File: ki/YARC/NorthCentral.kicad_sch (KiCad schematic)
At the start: 9 parts, among them U102 74HC245, U103 74HC245, U106 74LS139, U128 74LS157, U132 74LS157, U133 74LS21, U134 74LS32

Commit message: Ongoing corrections and improvements
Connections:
- net KX_HI_CLK renamed ~{KX_HI_OE}
- net KX_LO_CLK renamed ~{KX_LO_OE}
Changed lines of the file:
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@@
     )
   )
-  (global_label "KX_LO_CLK" (shape input) (at 203.2 73.66 0) (fields_autoplaced)
+  (global_label "~{KX_LO_OE}" (shape input) (at 203.2 73.66 0) (fields_autoplaced)
     (effects (font (size 1.27 1.27)) (justify left))
-    (property "Intersheet References" "${INTERSHEET_REFS}" (id 0) (at 215.9545 73.5806 0)
+    (property "Intersheet References" "${INTERSHEET_REFS}" (id 0) (at 214.866 73.5806 0)
       (effects (font (size 1.27 1.27)) (justify left) hide)
     )
@@
     )
   )
-  (global_label "KX_HI_CLK" (shape input) (at 203.2 88.9 0) (fields_autoplaced)
+  (global_label "~{KX_HI_OE}" (shape input) (at 203.2 88.9 0) (fields_autoplaced)
     (effects (font (size 1.27 1.27)) (justify left))
-    (property "Intersheet References" "${INTERSHEET_REFS}" (id 0) (at 215.5312 88.8206 0)
+    (property "Intersheet References" "${INTERSHEET_REFS}" (id 0) (at 214.4426 88.8206 0)
       (effects (font (size 1.27 1.27)) (justify left) hide)
     )

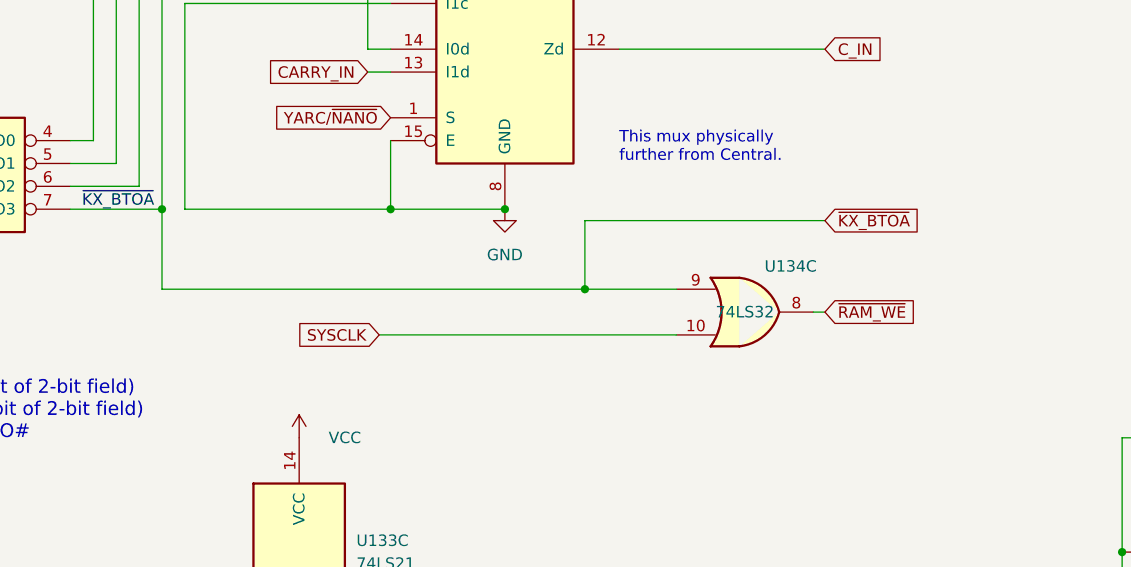
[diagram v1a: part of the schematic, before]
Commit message: Add the ACN mini-bus which can come from the instruction bits 11:8 or from the microcode bits 23:20. It selects the ALU operation and the condition codes.
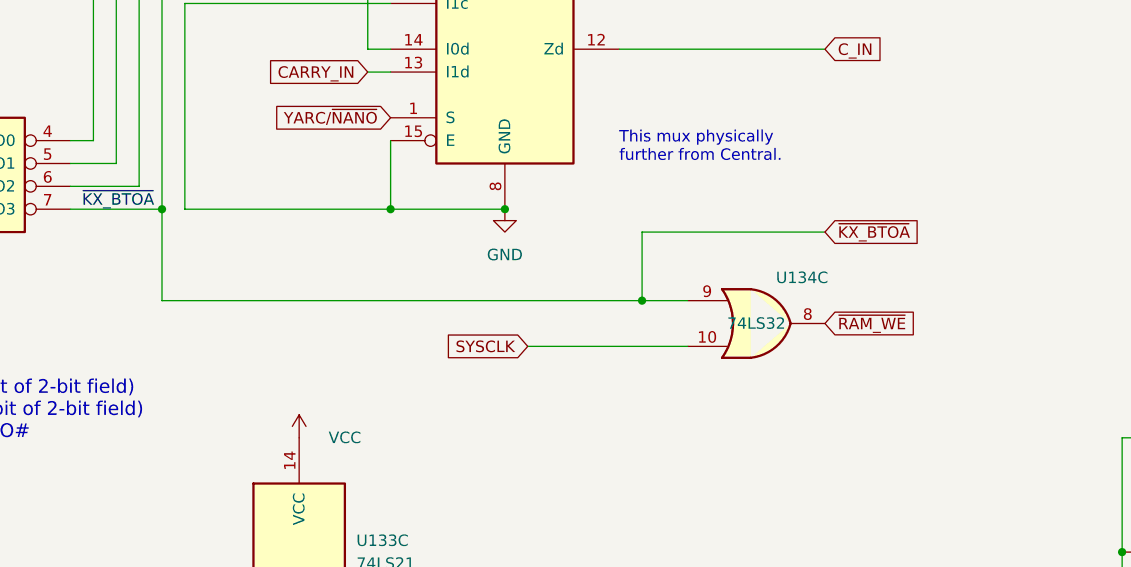
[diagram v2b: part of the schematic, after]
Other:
- moved on the sheet: U134C
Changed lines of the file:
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@@
   (junction (at 132.08 63.5) (diameter 0) (color 0 0 0 0)
   )
+  (junction (at 182.88 149.86) (diameter 0) (color 0 0 0 0)
+  )
   (junction (at 149.86 114.3) (diameter 0) (color 0 0 0 0)
   )
@@
   (junction (at 167.64 139.7) (diameter 0) (color 0 0 0 0)
   )
-  (junction (at 176.53 148.59) (diameter 0) (color 0 0 0 0)
-  )
   (junction (at 129.54 106.68) (diameter 0) (color 0 0 0 0)
   )
@@
     (stroke (width 0) (type default) (color 0 0 0 0))
   )
-  (wire (pts (xy 176.53 140.97) (xy 176.53 148.59))
-    (stroke (width 0) (type default) (color 0 0 0 0))
-  )
   (wire (pts (xy 119.38 139.7) (xy 129.54 139.7))
     (stroke (width 0) (type default) (color 0 0 0 0))
@@
     (stroke (width 0) (type default) (color 0 0 0 0))
   )
-  (wire (pts (xy 201.93 151.13) (xy 203.2 151.13))
-    (stroke (width 0) (type default) (color 0 0 0 0))
-  )
   (wire (pts (xy 134.62 101.6) (xy 134.62 91.44))
     (stroke (width 0) (type default) (color 0 0 0 0))
   )
+  (wire (pts (xy 187.96 154.94) (xy 170.18 154.94))
+    (stroke (width 0) (type default) (color 0 0 0 0))
+  )
   (wire (pts (xy 154.94 124.46) (xy 152.4 124.46))
     (stroke (width 0) (type default) (color 0 0 0 0))
@@
     (stroke (width 0) (type default) (color 0 0 0 0))
   )
+  (wire (pts (xy 187.96 149.86) (xy 182.88 149.86))
+    (stroke (width 0) (type default) (color 0 0 0 0))
+  )
   (wire (pts (xy 167.64 17.78) (xy 167.64 21.59))
     (stroke (width 0) (type default) (color 0 0 0 0))
@@
     (stroke (width 0) (type default) (color 0 0 0 0))
   )
-  (wire (pts (xy 186.69 148.59) (xy 176.53 148.59))
-    (stroke (width 0) (type default) (color 0 0 0 0))
-  )
   (bus (pts (xy 22.86 20.32) (xy 22.86 25.4))
     (stroke (width 0) (type default) (color 0 0 0 0))
@@
     (stroke (width 0) (type default) (color 0 0 0 0))
   )
+  (wire (pts (xy 182.88 142.24) (xy 182.88 149.86))
+    (stroke (width 0) (type default) (color 0 0 0 0))
+  )
   (wire (pts (xy 27.94 20.32) (xy 53.34 20.32))
     (stroke (width 0) (type default) (color 0 0 0 0))
@@
     (stroke (width 0) (type default) (color 0 0 0 0))
   )
+  (wire (pts (xy 203.2 142.24) (xy 182.88 142.24))
+    (stroke (width 0) (type default) (color 0 0 0 0))
+  )
   (bus (pts (xy 78.74 160.02) (xy 78.74 162.56))
     (stroke (width 0) (type default) (color 0 0 0 0))
@@
     (stroke (width 0) (type default) (color 0 0 0 0))
   )
-  (wire (pts (xy 129.54 148.59) (xy 129.54 139.7))
+  (wire (pts (xy 129.54 139.7) (xy 129.54 149.86))
     (stroke (width 0) (type default) (color 0 0 0 0))
   )
@@
     (stroke (width 0) (type default) (color 0 0 0 0))
   )
-  (wire (pts (xy 153.67 153.67) (xy 186.69 153.67))
-    (stroke (width 0) (type default) (color 0 0 0 0))
-  )
   (wire (pts (xy 81.28 139.7) (xy 93.98 139.7))
     (stroke (width 0) (type default) (color 0 0 0 0))
@@
     (stroke (width 0) (type default) (color 0 0 0 0))
   )
+  (wire (pts (xy 182.88 149.86) (xy 129.54 149.86))
+    (stroke (width 0) (type default) (color 0 0 0 0))
+  )
   (wire (pts (xy 152.4 121.92) (xy 152.4 114.3))
     (stroke (width 0) (type default) (color 0 0 0 0))
@@
     (stroke (width 0) (type default) (color 0 0 0 0))
   )
-  (wire (pts (xy 176.53 148.59) (xy 129.54 148.59))
-    (stroke (width 0) (type default) (color 0 0 0 0))
-  )
   (bus (pts (xy 22.86 172.72) (xy 22.86 193.04))
     (stroke (width 0) (type default) (color 0 0 0 0))
@@
   )
   (wire (pts (xy 76.2 45.72) (xy 66.04 45.72))
-    (stroke (width 0) (type default) (color 0 0 0 0))
-  )
-  (wire (pts (xy 203.2 140.97) (xy 176.53 140.97))
     (stroke (width 0) (type default) (color 0 0 0 0))
   )
@@
     )
   )
-  (global_label "SYSCLK" (shape input) (at 153.67 153.67 180) (fields_autoplaced)
-    (effects (font (size 1.27 1.27)) (justify right))
-    (property "Intersheet References" "${INTERSHEET_REFS}" (id 0) (at 144.1812 153.5906 0)
+  (global_label "SYSCLK" (shape input) (at 170.18 154.94 180) (fields_autoplaced)
+    (effects (font (size 1.27 1.27)) (justify right))
+    (property "Intersheet References" "${INTERSHEET_REFS}" (id 0) (at 160.6912 154.8606 0)
       (effects (font (size 1.27 1.27)) (justify right) hide)
     )
@@
     )
   )
-  (global_label "~{KX_BTOA}" (shape input) (at 203.2 140.97 0) (fields_autoplaced)
-    (effects (font (size 1.27 1.27)) (justify left))
-    (property "Intersheet References" "${INTERSHEET_REFS}" (id 0) (at 213.7169 140.8906 0)
+  (global_label "~{KX_BTOA}" (shape input) (at 203.2 142.24 0) (fields_autoplaced)
+    (effects (font (size 1.27 1.27)) (justify left))
+    (property "Intersheet References" "${INTERSHEET_REFS}" (id 0) (at 213.7169 142.1606 0)
       (effects (font (size 1.27 1.27)) (justify left) hide)
     )
@@
     )
   )
-  (global_label "~{RAM_WE}" (shape input) (at 203.2 151.13 0) (fields_autoplaced)
-    (effects (font (size 1.27 1.27)) (justify left))
-    (property "Intersheet References" "${INTERSHEET_REFS}" (id 0) (at 212.9912 151.0506 0)
+  (global_label "~{RAM_WE}" (shape input) (at 203.2 152.4 0) (fields_autoplaced)
+    (effects (font (size 1.27 1.27)) (justify left))
+    (property "Intersheet References" "${INTERSHEET_REFS}" (id 0) (at 212.9912 152.3206 0)
       (effects (font (size 1.27 1.27)) (justify left) hide)
     )
@@
     (pin "7")
   )
-  (symbol (lib_id "74xx:74LS32") (at 194.31 151.13 0) (unit 3)
+  (symbol (lib_id "74xx:74LS32") (at 195.58 152.4 0) (unit 3)
     (in_bom yes) (on_board yes)
-    (property "Reference" "U134" (id 0) (at 199.39 146.05 0))
-    (property "Value" "74LS32" (id 1) (at 194.31 151.13 0))
-    (property "Footprint" "" (id 2) (at 194.31 151.13 0)
-      (effects (font (size 1.27 1.27)) hide)
-    )
-    (property "Datasheet" "http://www.ti.com/lit/gpn/sn74LS32" (id 3) (at 194.31 151.13 0)
-      (effects (font (size 1.27 1.27)) hide)
-    )
+    (property "Reference" "U134" (id 0) (at 200.66 147.32 0))
+    (property "Value" "74LS32" (id 1) (at 195.58 152.4 0))
+    (property "Footprint" "" (id 2) (at 195.58 152.4 0)
+      (effects (font (size 1.27 1.27)) hide)
+    )
+    (property "Datasheet" "http://www.ti.com/lit/gpn/sn74LS32" (id 3) (at 195.58 152.4 0)
+      (effects (font (size 1.27 1.27)) hide)
+    )

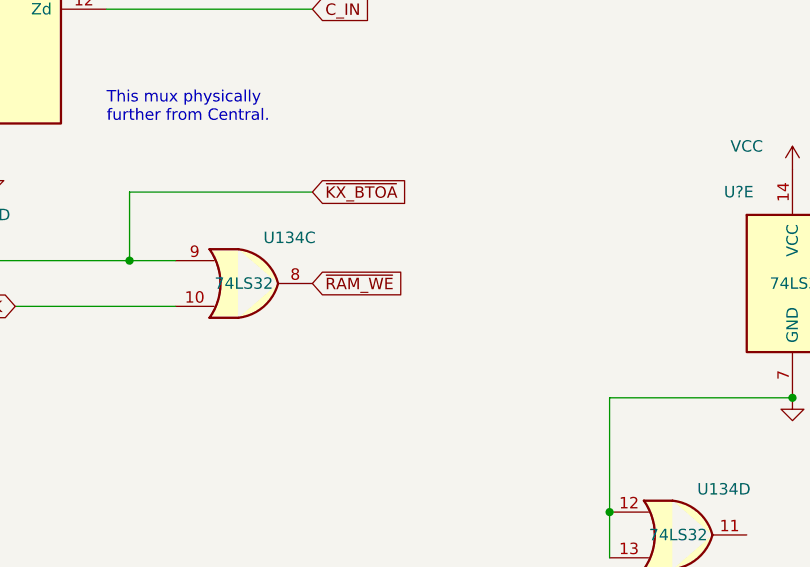
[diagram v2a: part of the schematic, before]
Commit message: Ongoing corrections. Document the Nano's sysbus enable control for the first time.
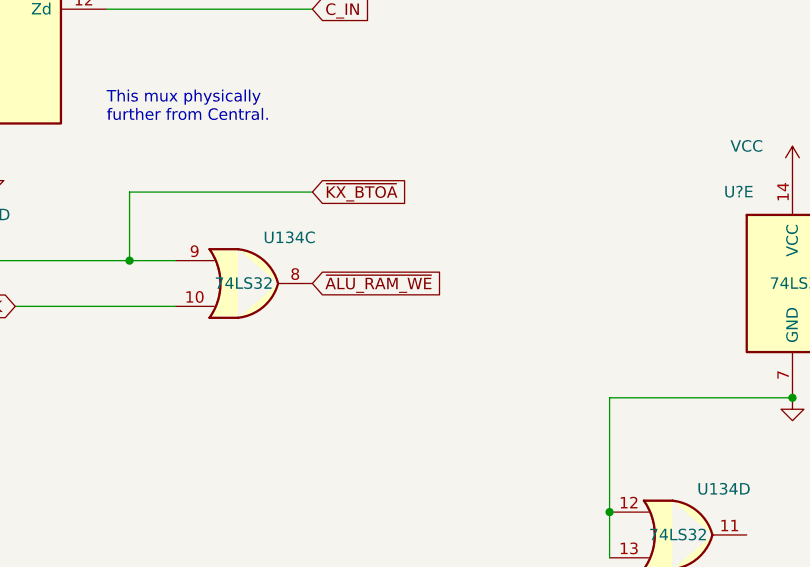
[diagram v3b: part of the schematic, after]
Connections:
- net ~{RAM_WE} renamed ~{ALU_RAM_WE}
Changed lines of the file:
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@@
     )
   )
-  (global_label "~{RAM_WE}" (shape input) (at 203.2 152.4 0) (fields_autoplaced)
+  (global_label "~{ALU_RAM_WE}" (shape input) (at 203.2 152.4 0) (fields_autoplaced)
     (effects (font (size 1.27 1.27)) (justify left))
-    (property "Intersheet References" "${INTERSHEET_REFS}" (id 0) (at 212.9912 152.3206 0)
+    (property "Intersheet References" "${INTERSHEET_REFS}" (id 0) (at 217.406 152.3206 0)
       (effects (font (size 1.27 1.27)) (justify left) hide)
     )

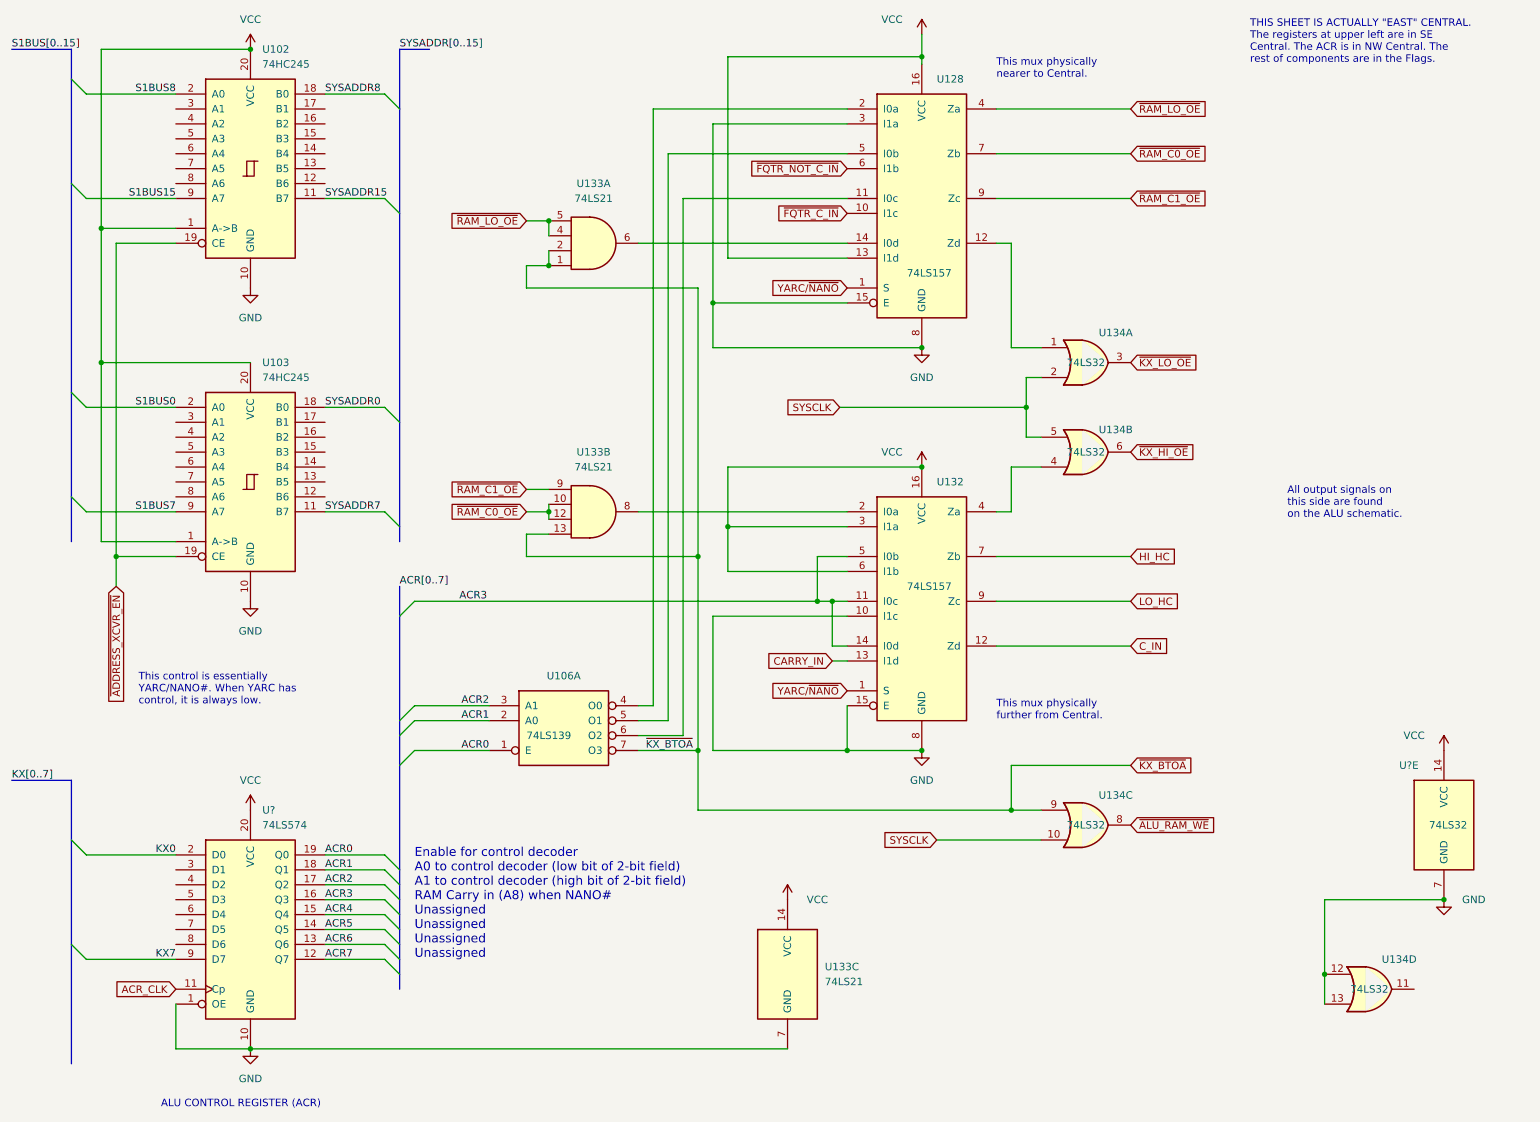
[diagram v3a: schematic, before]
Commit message: Document ALU RAM write clock delay line (fix for ALU RAM write issue)
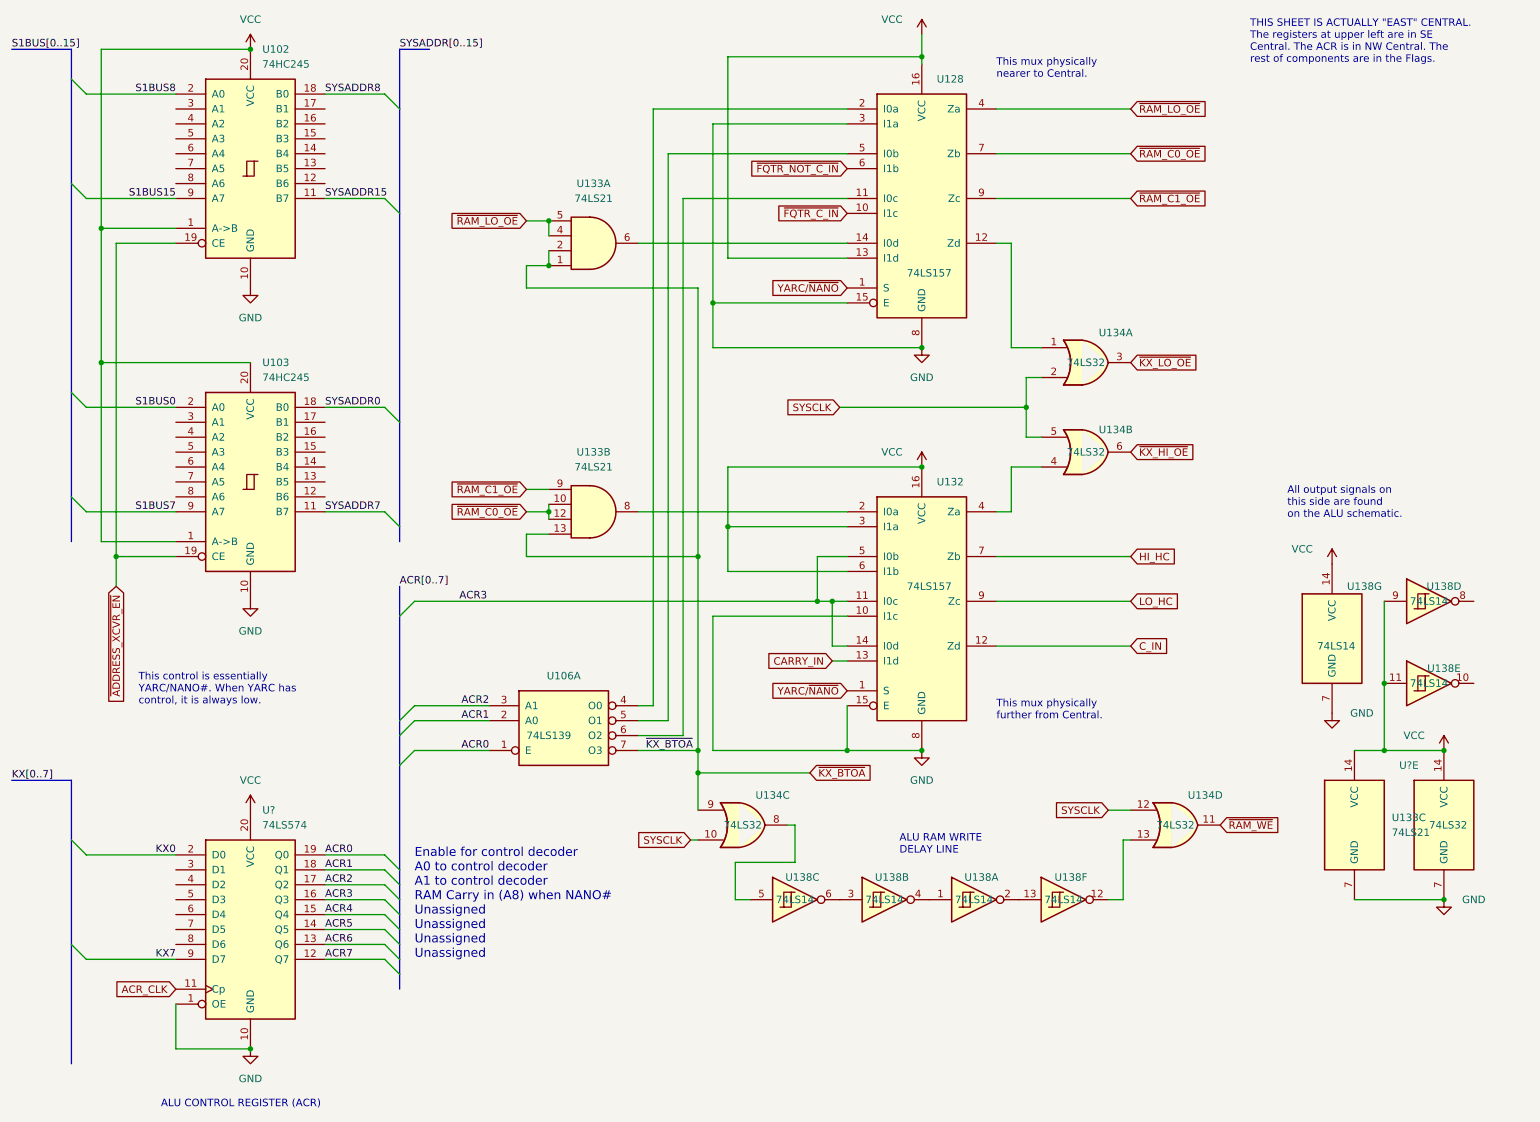
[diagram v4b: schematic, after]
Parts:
- added U138: 74LS14, symbol 74xx:74LS14
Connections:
- net GND: now also U138.7 (GND); no longer U134.12, U134.13
- net SYSCLK: now also U134.12
- net VCC: now also U138.11, U138.14 (VCC), U138.9
- net ~{RAM_WE}: now reaches U134.11
- net ~{ALU_RAM_WE}: no longer names the net of U134.8
- net ~{ALU_RAM_WE}: now also U138.5
- new net: U138.3, U138.6
- new net: U138.1, U138.4
- new net: U134.13, U138.12
- new net: U138.13, U138.2
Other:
- note added: "ALU RAM WRITE DELAY LINE"
- note added: "Enable for control decoder A0 to control decoder A1 to control decoder RAM Carry in (A8) when NANO# Unassigned Unassigned Unassigned Unassigned"
- note removed: "Enable for control decoder A0 to control decoder (low bit of 2-bit field) A1 to control decoder (high bit of 2-bit field) RAM Carry in (A8) when NANO# Unassigned Unassigned Unassigned Unassigned"
- moved on the sheet: U133C, U134C, U134D
